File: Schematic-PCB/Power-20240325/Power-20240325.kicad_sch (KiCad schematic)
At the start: 23 parts, among them J1 Conn_01x02_Pin, J3 Conn_01x02_Pin, J4 Conn_01x02_Pin, J5 Conn_01x03_Pin, J6 Conn_01x02_Pin, SW1 SW_DPST_x2

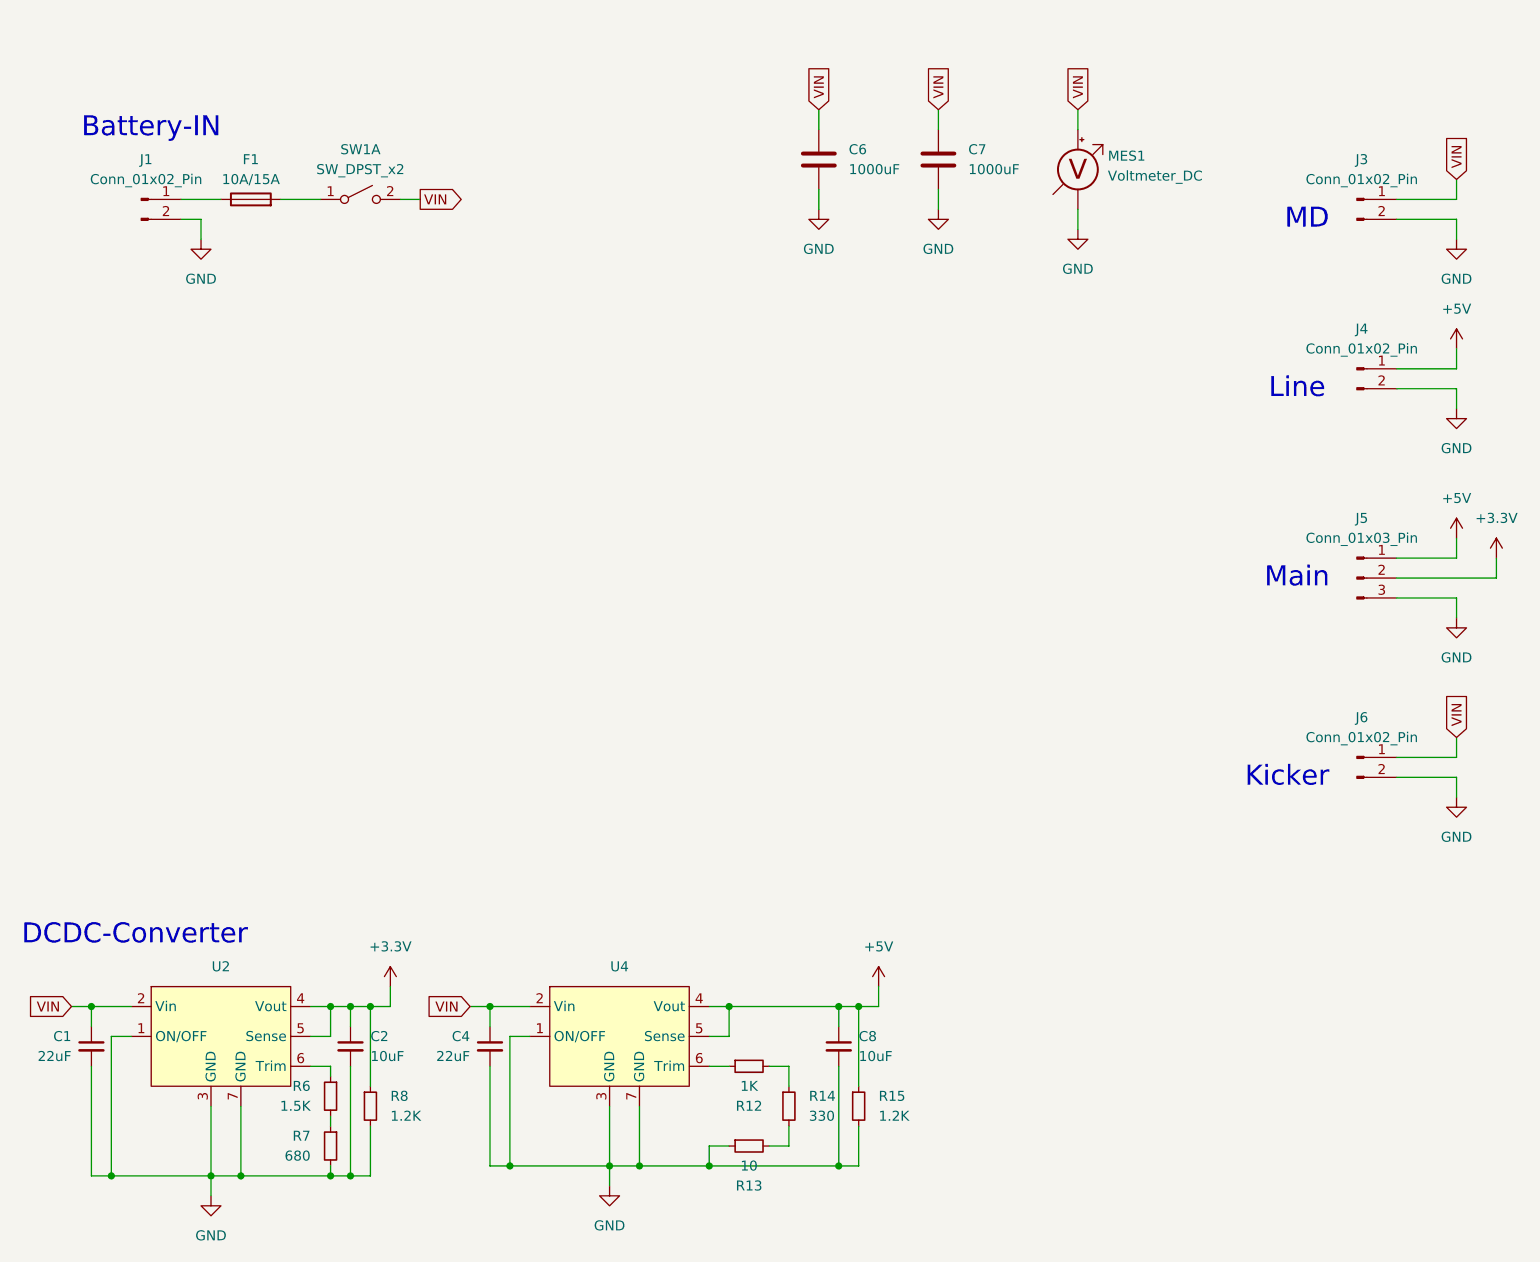
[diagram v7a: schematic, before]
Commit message: 電源基板を更新
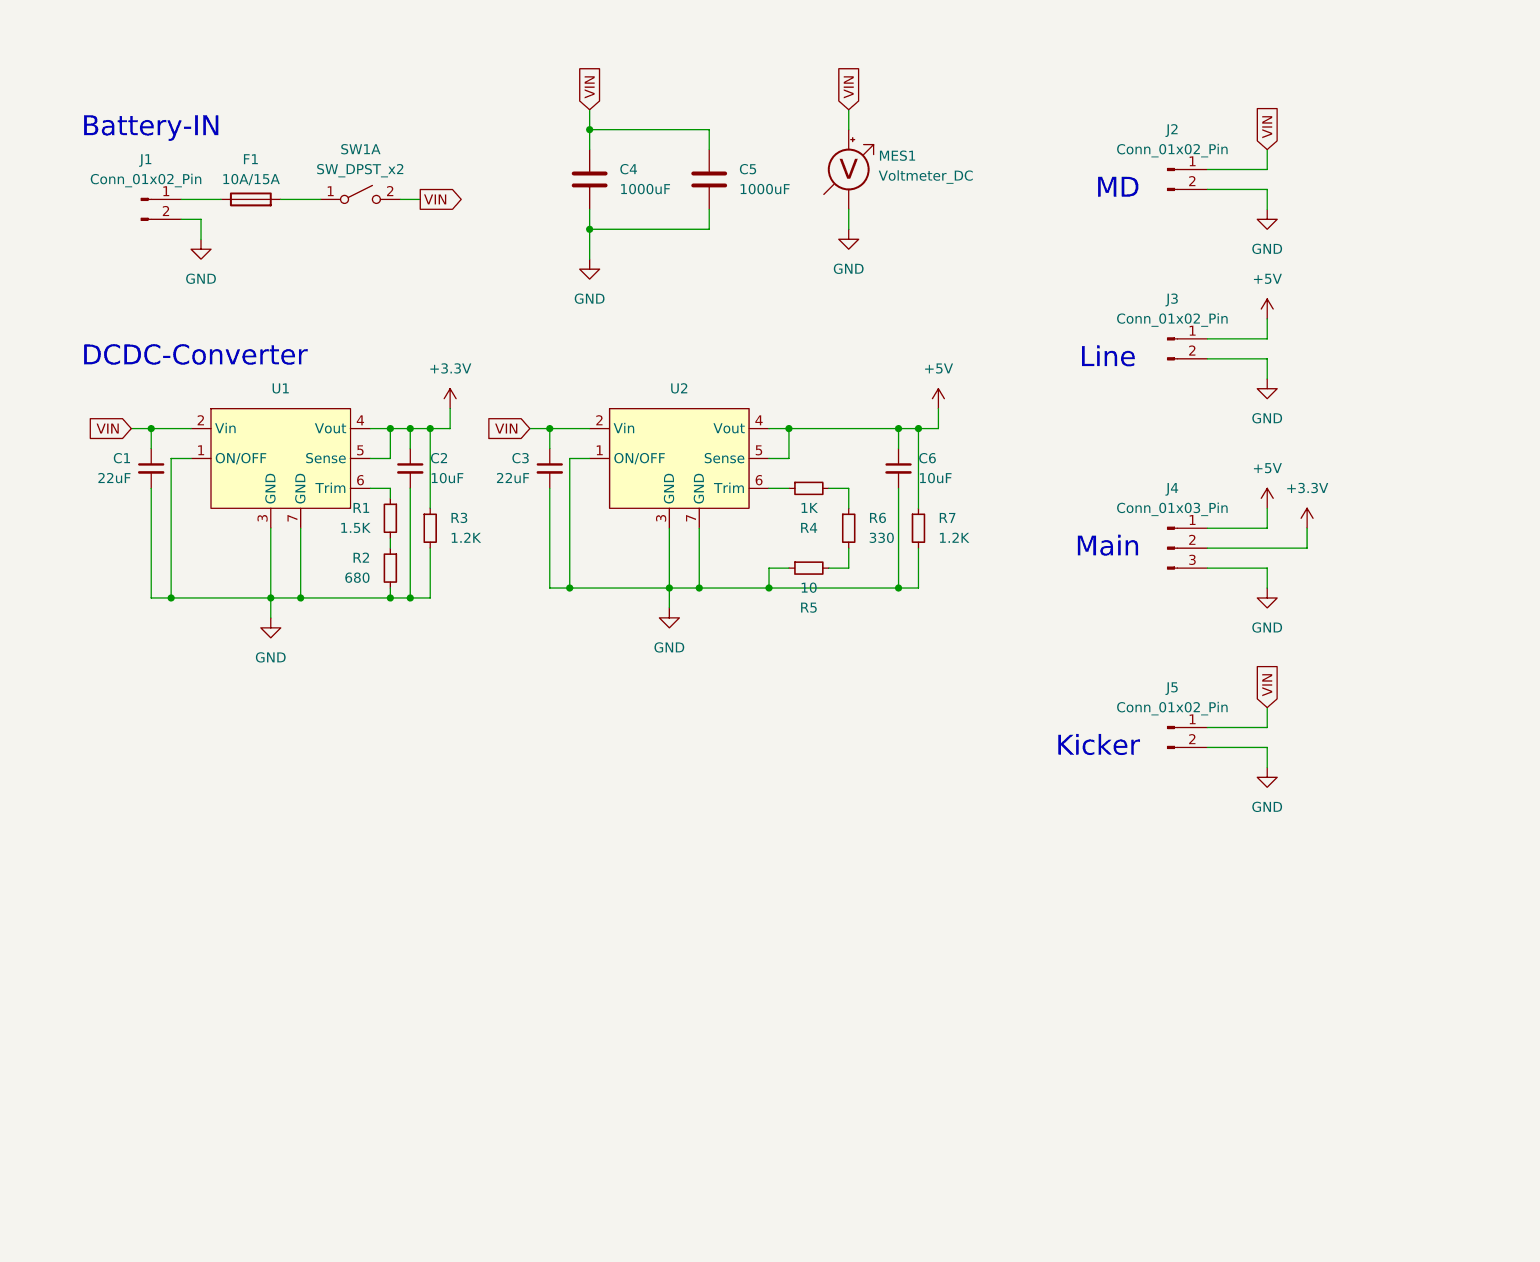
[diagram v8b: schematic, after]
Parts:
- J1: footprint Connector_JST:JST_VH_B2P-VH-B_1x02_P3.96mm_Vertical -> @2024-Power:VIN
- SW1: footprint (none) -> @2024-Power:RA1113112R
- renumbered C4 to C3, C6 to C4, C7 to C5, C8 to C6, J3 to J2, J4 to J3, J5 to J4, J6 to J5, R6 to R1, R7 to R2, R8 to R3, R12 to R4, R13 to R5, R14 to R6, R15 to R7, U2 to U1, U4 to U2
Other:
- moved on the sheet: C1, C2, C3, C4, C5, C6, J2, J3, J4, J5, MES1, R1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
